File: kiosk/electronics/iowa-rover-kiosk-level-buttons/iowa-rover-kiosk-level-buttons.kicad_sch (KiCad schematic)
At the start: 26 parts, among them J1 Conn_02x08_Top_Bottom, SW1 SW_Push, SW2 SW_Push, SW3 SW_Push, SW4 SW_Push, SW5 SW_Push, SW6 SW_Push, SW7 SW_Push, SW8 SW_Push, U1 TPIC6A595NE

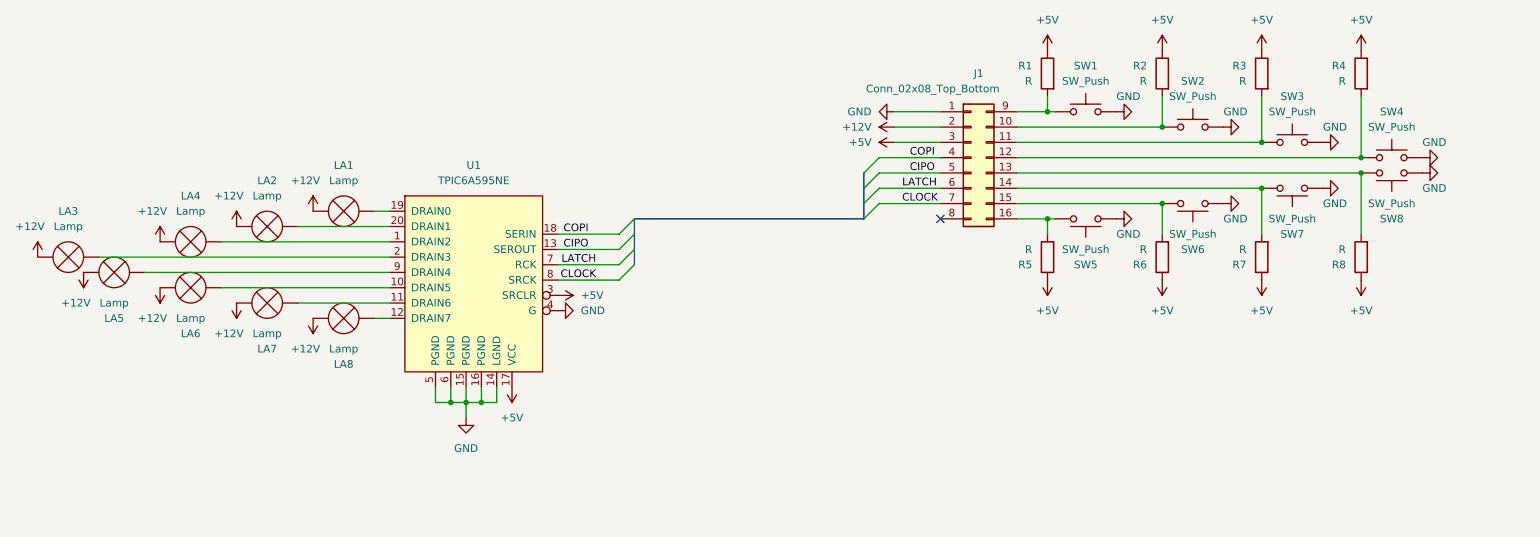
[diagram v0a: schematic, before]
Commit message: initial pass at board drawings
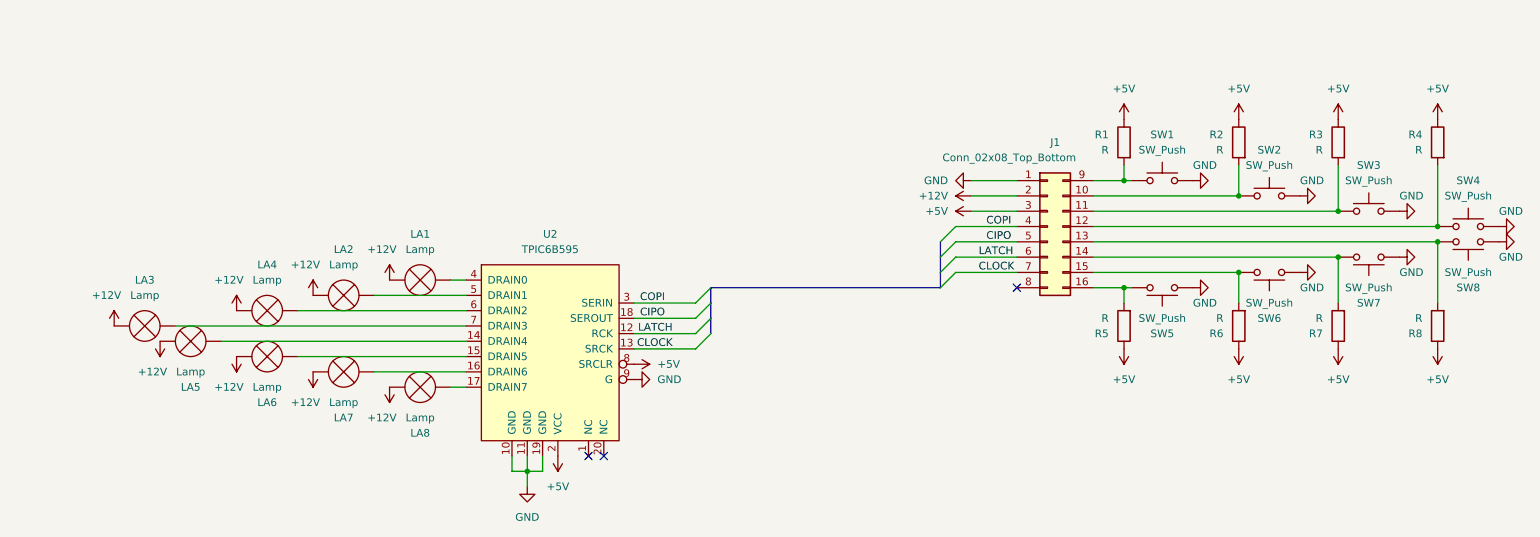
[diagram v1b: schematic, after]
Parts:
- removed U1: TPIC6A595NE, symbol SMM:TPIC6A595NE
- added U2: TPIC6B595, Package_DIP:DIP-20_W7.62mm, symbol SMM:TPIC6B595
- J1: footprint (none) -> Connector_PinHeader_2.54mm:PinHeader_2x08_P2.54mm_Vertical
- LA1, LA2, LA3, LA4, LA5, LA6, LA7, LA8, SW1, SW2, SW3, SW4, SW5, SW6, SW7, SW8: footprint (none) -> SMM:TerminalBlock-2_P5.08mm_small
- R1, R2, R3, R4, R5, R6, R7, R8: footprint (none) -> SMM:Resistor_L6.3mm_D2.5mm_P10.16mm_Horizontal
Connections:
- net +5V: now also U2.2 (VCC), U2.8 (SRCLR)
- net CIPO: now also U2.18 (SEROUT)
- net CLOCK: now also U2.13 (SRCK)
- net COPI: now also U2.3 (SERIN)
- net GND: now also U2.10 (GND), U2.11 (GND), U2.19 (GND), U2.9 (G)
- net LATCH: now also U2.12 (RCK)
- net at LA7.1 (-): now also U2.16 (DRAIN6)
- net at LA4.1 (-): now also U2.6 (DRAIN2)
- net at LA6.1 (-): now also U2.15 (DRAIN5)
- net at LA8.1 (-): now also U2.17 (DRAIN7)
- net at LA1.1 (-): now also U2.4 (DRAIN0)
- net at LA3.1 (-): now also U2.7 (DRAIN3)
- net at LA2.1 (-): now also U2.5 (DRAIN1)
- net at LA5.1 (-): now also U2.14 (DRAIN4)
- no-connect marks 1 -> 3
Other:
- moved on the sheet: J1, LA1, LA2, LA3, LA4, LA5, LA6, LA7, LA8, R1, R2, R3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

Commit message: update
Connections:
- net +12V: no longer LA1.2 (+), LA2.2 (+), LA3.2 (+), LA4.2 (+), LA5.2 (+), LA6.2 (+), LA7.2 (+), LA8.2 (+)
- net +5V: now also LA1.2 (+), LA2.2 (+), LA3.2 (+), LA4.2 (+), LA5.2 (+), LA6.2 (+), LA7.2 (+), LA8.2 (+)

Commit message: add pdf schematics
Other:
- company: (none) -> Science Museum of Minnesota
- title: (none) -> Iowa Science Rover Kiosk - Level Buttons Board
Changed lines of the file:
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@@
 (kicad_sch (version 20230121) (generator eeschema)
   (paper "A4")
+  (title_block
+    (title "Iowa Science Rover Kiosk - Level Buttons Board")
+    (date "2023-10-05")
+    (rev "0")
+    (company "Science Museum of Minnesota")
+    (comment 1 "Kate Swanson")
+  )
   (junction (at 246.38 76.2) (diameter 0) (color 0 0 0 0)
   )
